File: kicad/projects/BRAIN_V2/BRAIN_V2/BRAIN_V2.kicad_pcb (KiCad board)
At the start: 4 copper layers, 75 x 70 mm, 64 parts, among them J1 Conn_ARM_JTAG_SWD_10, J2 UART, J3 USB_C_Receptacle_USB2.0_16P, J5 I2C, J6 Conn_02x11_Odd_Even, J7 Conn_02x04_Odd_Even, J8 Conn_02x06_Odd_Even, J9 USB_C_Receptacle_USB2.0_16P, Q1 BC847, SW1 TL3342F450QG, U1 24LC512, U3 AP2112K-3.3, U4 AP2112K-3.3, U73 STM32L433CCTx, Y1 NX3215SA-32.768KHZ-EXS00A-MU0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

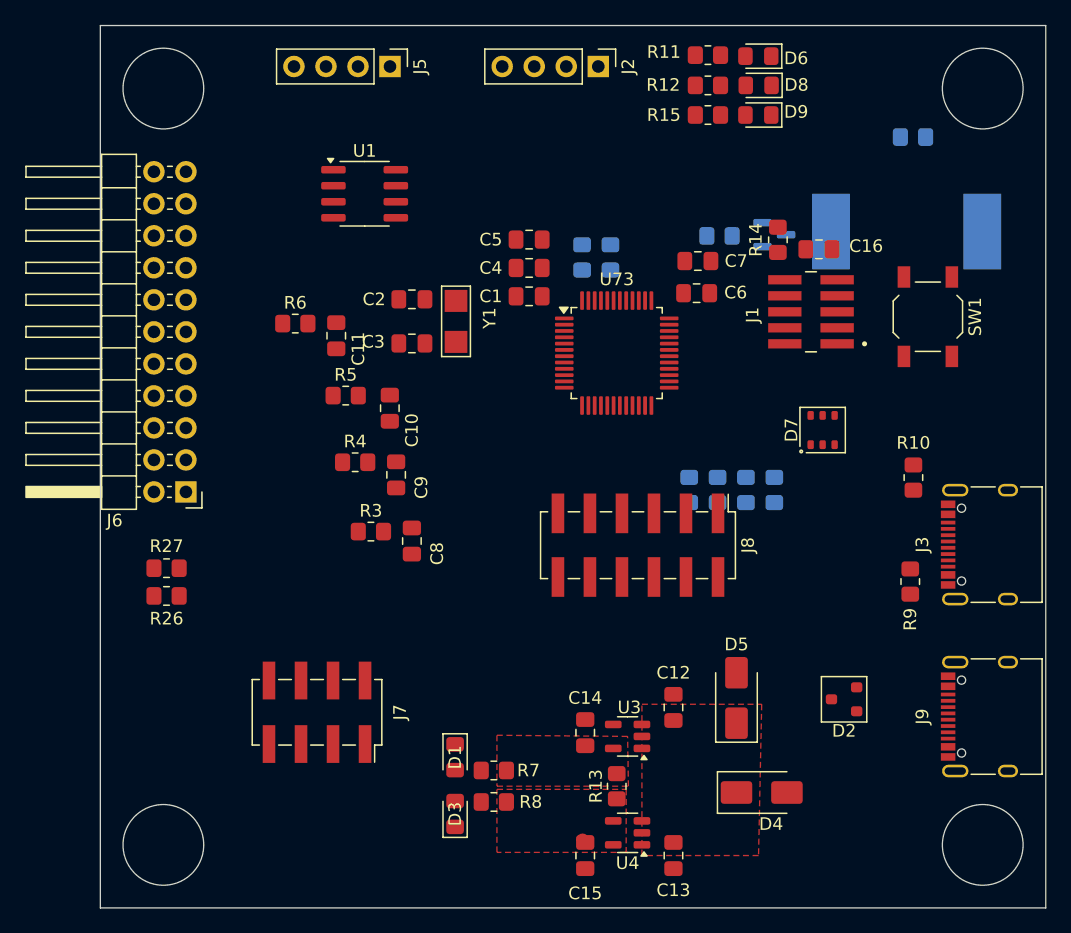
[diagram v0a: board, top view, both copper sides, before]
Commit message: brain v2 connections
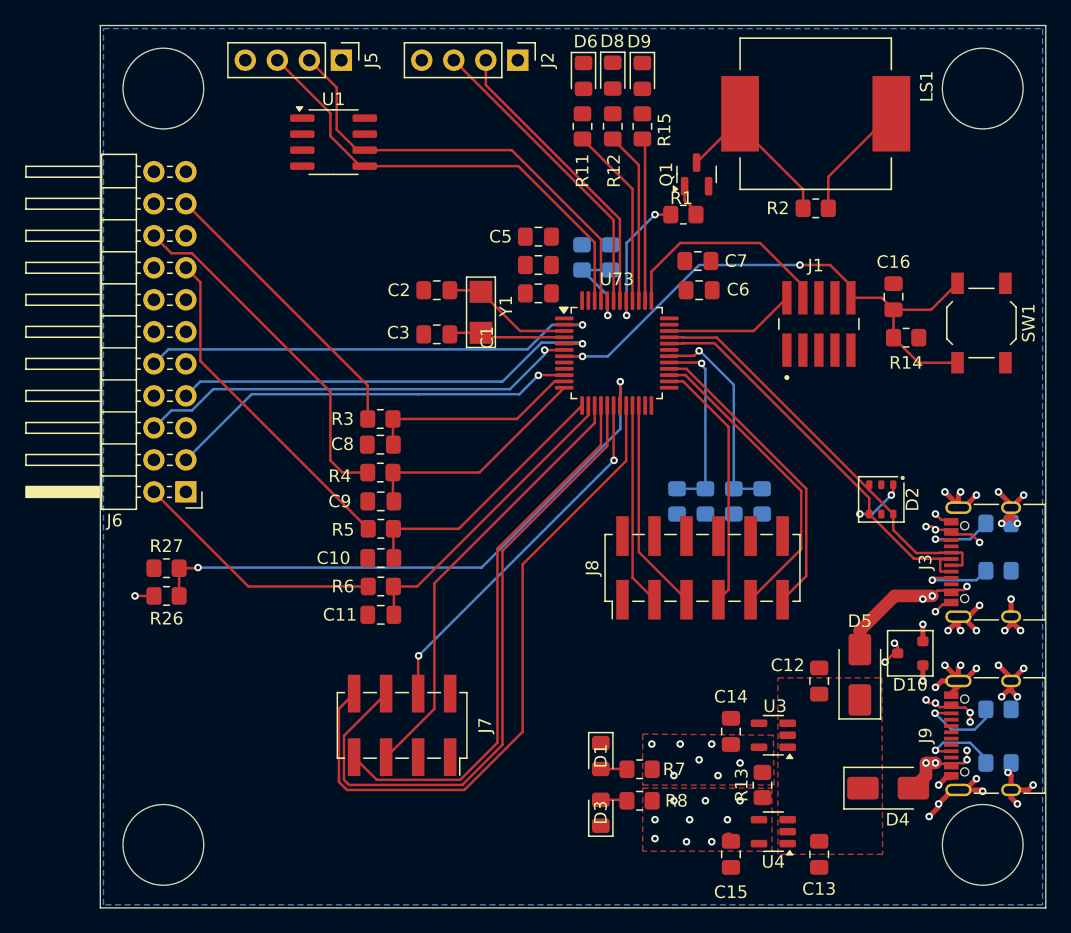
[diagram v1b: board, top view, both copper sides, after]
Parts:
- removed D7: TVS3V3L4U, PCM_Package_SO_AKL:TSOP-6_1.65x3.05mm_P0.95mm
- added D10: PESD5V0L2BT, PCM_Package_TO_SOT_SMD_AKL:SOT-23, F.Cu at (114.2, 119.8)
- added R16: 5.1k, Resistor_SMD:R_0805_2012Metric_Pad1.20x1.40mm_HandSolder, B.Cu at (121.2, 128.5)
- added R17: 5.1k, Resistor_SMD:R_0805_2012Metric_Pad1.20x1.40mm_HandSolder, B.Cu at (121.2, 124.2)
- D2: value PESD5V0L2BT -> TVS3V3L4U; footprint PCM_Package_TO_SOT_SMD_AKL:SOT-23 -> PCM_Package_SO_AKL:TSOP-6_1.65x3.05mm_P0.95mm
- LS1, Q1, R1, R2: moved to F.Cu
- R10, R9: moved to B.Cu
- moved C11 22.4 mm to (72.2, 116.8), turned to 180 degrees
- moved R6 21.9 mm to (72.2, 114.5)
- moved D2 16.1 mm to (112.0, 107.6), turned to -90 degrees
- moved D6 14.0 mm to (88.3, 74.0), turned to -90 degrees
- moved R14 12.8 mm to (113.9, 94.8), turned to 180 degrees
- moved C10 11.9 mm to (72.2, 112.2), turned to 180 degrees
- moved LS1 11.8 mm to (106.8, 77.0), turned to -90 degrees
- moved C12 11.7 mm to (107.0, 122.0)
- moved D8 11.6 mm to (90.7, 74.0), turned to -90 degrees
- moved C13 11.6 mm to (107.0, 135.8)
- moved C14 11.6 mm to (100.0, 126.0)
- moved C15 11.6 mm to (100.0, 135.8)
- moved D1 11.6 mm to (89.7, 128.0)
- moved D3 11.6 mm to (89.7, 132.4)
- moved R13 11.6 mm to (102.5, 130.2)
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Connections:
- D2 pad 1: Net-(D2-A1) -> USB_N
- D2 pad 2: 5V_USB -> unconnected-(D2-VN-Pad2)
- D2 pad 3: GND -> USB_P
- D4 pad 2: Net-(D2-A1) -> Net-(D10-A1)
- D5 pad 2: 5V_USB -> Net-(D10-A2)
- J3 pad A4: 5V_USB -> Net-(D10-A2)
- J3 pad A9: 5V_USB -> Net-(D10-A2)
- J3 pad B4: 5V_USB -> Net-(D10-A2)
- J3 pad B9: 5V_USB -> Net-(D10-A2)
- J6 pad 14: FBK_3V3_SENSORS_EXT -> unconnected-(J6-Pin_14-Pad14)
- J9 pad A4: Net-(D2-A1) -> Net-(D10-A1)
- J9 pad A5: unconnected-(J9-CC1-PadA5) -> Net-(J9-CC1)
- J9 pad A9: Net-(D2-A1) -> Net-(D10-A1)
- J9 pad B4: Net-(D2-A1) -> Net-(D10-A1)
- J9 pad B5: unconnected-(J9-CC2-PadB5) -> Net-(J9-CC2)
- J9 pad B9: Net-(D2-A1) -> Net-(D10-A1)
- R3 pad 1: SIG1 -> SIG4
- R4 pad 1: SIG2 -> SIG3
- R5 pad 1: SIG3 -> SIG2
- R6 pad 1: SIG4 -> SIG1
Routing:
- net GND: track 0.00 -> 54.1 mm, vias 0 -> 34
- net NRF24_IRQ: track 0.00 -> 53.5 mm
- net NRF24_MOSI: track 0.00 -> 52.6 mm
- net FBK_3V3_SENSORS: track 0.00 -> 47.5 mm, vias 0 -> 2
- net NRST: track 0.00 -> 45.2 mm, vias 0 -> 2
- net NRF24_MISO: track 0.00 -> 43.5 mm
- net USB_N: track 0.00 -> 37.7 mm, vias 0 -> 2
- net I2C_DATA: track 0.00 -> 36.8 mm
- net MUX4: track 0.00 -> 36.7 mm, vias 0 -> 1
- net I2C_CLK: track 0.00 -> 35.8 mm
- net MUX2: track 0.00 -> 35.3 mm, vias 0 -> 1
- net NRF24_SCK: track 0.00 -> 34.7 mm
- net MUX3: track 0.00 -> 34.7 mm, vias 0 -> 1
- net USB_P: track 0.00 -> 33.3 mm
- net MUX1: track 0.00 -> 32.8 mm, vias 0 -> 1
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- added copper zone on In2.Cu, net 3V3_OUT
- added copper zone on B.Cu, net GND
- added copper zone on In2.Cu, net Net-(D10-A1)
- added copper zone on In2.Cu, net Net-(D10-A2)

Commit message: brain v2 connections
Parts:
- moved R26 36.5 mm to (85.8, 135.2), turned to -90 degrees
- moved R27 36.0 mm to (83.5, 135.2), turned to -90 degrees
- moved J6 21.8 mm to (56.8, 128.8)
- moved C4 18.7 mm to (96.2, 103.8), turned to 0 degrees
- moved C1 15.4 mm to (96.2, 101.5), turned to 0 degrees
- moved C5 4.03 mm to (85.3, 90.8), turned to 90 degrees
- moved C6 0.90 mm to (97.0, 91.8)
- moved C7 0.85 mm to (97.0, 89.4)
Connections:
- U73 pad 10: MUX1 -> MUX4
- U73 pad 2: MUX4 -> MUX1
- U73 pad 5: MUX3 -> MUX2
- U73 pad 6: MUX2 -> MUX3
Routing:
- net +3V3: track 9.57 -> 77.6 mm, vias 7 -> 24
- net 5V_IN: track 0.00 -> 60.5 mm, vias 0 -> 26
- net NRF24_CE: track 0.00 -> 41.6 mm, vias 0 -> 2
- net 3V3_OUT_EN: track 0.00 -> 40.7 mm, vias 0 -> 2
- net MUX1: track 32.8 -> 65.3 mm, vias 1 -> 0
- net MUX2: track 35.3 -> 59.5 mm, vias 1 -> 0
- net MUX3: track 34.7 -> 58.1 mm, vias 1 -> 0
- net MUX4: track 36.7 -> 52.0 mm, vias 1 -> 0
- net 3V3_OUT: track 1.89 -> 14.8 mm, vias 10 -> 7
- net SIG2: track 26.7 -> 14.9 mm
- net SIG3: track 27.9 -> 18.2 mm
- net SIG4: track 23.0 -> 16.4 mm
- net FBK_3V3_SENSORS: track 47.5 -> 41.5 mm
- net Net-(U73-PC15): track 9.27 -> 12.9 mm, vias 0 -> 2
- net Net-(U73-PC14): track 10.4 -> 13.3 mm, vias 0 -> 2
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- added copper zone on In2.Cu, net 5V_IN
- added copper zone on F.Cu, net GND
- removed copper zone on F.Cu, net +3V3
- removed copper zone on F.Cu, net 3V3_OUT
- removed copper zone on F.Cu, net 5V_IN

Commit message: hw revisions and versions in schematic and pins
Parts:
- removed C2, C3: 3.9pF, Capacitor_SMD:C_0805_2012Metric_Pad1.18x1.45mm_HandSolder
- removed J8: Conn_02x06_Odd_Even, Connector_PinHeader_2.54mm:PinHeader_2x06_P2.54mm_Vertical_SMD
- removed R24, R25: 10k, Resistor_SMD:R_0805_2012Metric_Pad1.20x1.40mm_HandSolder
- removed Y1: NX3215SA-32.768KHZ-EXS00A-MU00525, PCM_Crystal_AKL:Crystal_SMD_MicroCrystal_CC7V-T1A-2Pin_3.2x1.5mm_HandSoldering
- added J4: Conn_02x03_Odd_Even, Connector_PinHeader_2.54mm:PinHeader_2x03_P2.54mm_Vertical_SMD, F.Cu at (93.5, 117.5)
- added R18: 10k, Resistor_SMD:R_0805_2012Metric_Pad1.20x1.40mm_HandSolder, F.Cu at (61.2, 119.0)
- added R19: 10k, Resistor_SMD:R_0805_2012Metric_Pad1.20x1.40mm_HandSolder, F.Cu at (59.8, 134.5)
- added R28: 10k, Resistor_SMD:R_0805_2012Metric_Pad1.20x1.40mm_HandSolder, F.Cu at (64.2, 134.5)
- added R29: 10k, Resistor_SMD:R_0805_2012Metric_Pad1.20x1.40mm_HandSolder, F.Cu at (62.0, 134.5)
- added R30: 10k, Resistor_SMD:R_0805_2012Metric_Pad1.20x1.40mm_HandSolder, F.Cu at (61.2, 117.0)
- added R31: 47k, Resistor_SMD:R_0805_2012Metric_Pad1.20x1.40mm_HandSolder, F.Cu at (61.8, 111.5)
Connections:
- J6 pad 10: MUX4 -> MUX2
- J6 pad 11: 3V3_OUT -> MUX3
- J6 pad 12: 3V3_OUT -> MUX4
- J6 pad 13: GND -> 3V3_OUT
- J6 pad 14: unconnected-(J6-Pin_14-Pad14) -> 3V3_OUT
- J6 pad 15: SIG2 -> GND
- J6 pad 16: GND -> FBK_3V3_SENSORS
- J6 pad 17: GND -> SIG2
- J6 pad 18: SIG3 -> GND
- J6 pad 19: SIG4 -> GND
- J6 pad 20: GND -> SIG3
- J6 pad 21: GND -> SIG4
- J6 pad 3: MUX1 -> SENSORS_REV0
- J6 pad 4: GND -> SENSORS_REV1
- J6 pad 5: GND -> SENSORS_HW_ID0
- J6 pad 6: MUX2 -> SENSORS_HW_ID1
- J6 pad 7: MUX3 -> 3V3_OUT
- J6 pad 8: GND -> SENSORS_HW_ID2
- J6 pad 9: 3V3_OUT -> MUX1
- R26 pad 1: FBK_3V3_SENSORS -> FBK_3V3_BRAIN
- R27 pad 1: FBK_3V3_SENSORS -> FBK_3V3_BRAIN
- U73 pad 10: MUX4 -> FBK_3V3_SENSORS
- U73 pad 19: FBK_3V3_SENSORS -> FBK_3V3_BRAIN
- U73 pad 26: EXPANSION2 -> SENSORS_HW_ID0
- U73 pad 27: EXPANSION3 -> SENSORS_HW_ID1
- U73 pad 28: EXPANSION4 -> SENSORS_HW_ID2
- U73 pad 3: Net-(U73-PC14) -> MUX2
- U73 pad 4: Net-(U73-PC15) -> MUX3
- U73 pad 44: HWREV2 -> SENSORS_REV1
- U73 pad 5: MUX2 -> MUX4
- U73 pad 6: MUX3 -> SENSORS_REV0
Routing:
- net SENSORS_REV1: track 0.00 -> 87.2 mm, vias 0 -> 2
- net SENSORS_HW_ID1: track 0.00 -> 73.3 mm, vias 0 -> 2
- net SENSORS_REV0: track 0.00 -> 73.2 mm, vias 0 -> 1
- net SENSORS_HW_ID2: track 0.00 -> 72.3 mm, vias 0 -> 1
- net SENSORS_HW_ID0: track 0.00 -> 67.0 mm, vias 0 -> 2
- net FBK_3V3_BRAIN: track 0.00 -> 38.7 mm, vias 0 -> 2
- net EXPANSION3: track 24.6 -> 0.00 mm
- net EXPANSION4: track 24.4 -> 0.00 mm
- net EXPANSION2: track 20.2 -> 0.00 mm
- net 3V3_OUT: track 14.8 -> 30.2 mm, vias 7 -> 8
- net Net-(U73-PC14): track 13.3 -> 0.00 mm, vias 2 -> 0
- net Net-(U73-PC15): track 12.9 -> 0.00 mm, vias 2 -> 0
- net FBK_3V3_SENSORS: track 41.5 -> 51.6 mm, vias 2 -> 0
- net HWREV2: track 7.89 -> 0.00 mm, vias 1 -> 0
- net MUX1: track 65.3 -> 60.8 mm
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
